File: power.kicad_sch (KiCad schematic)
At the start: 55 parts, among them T1 net-tie, U1 LMR54410, U11 RT9080-33GJ5, U3 TPS546D24ARVFR, U5 MIC5504

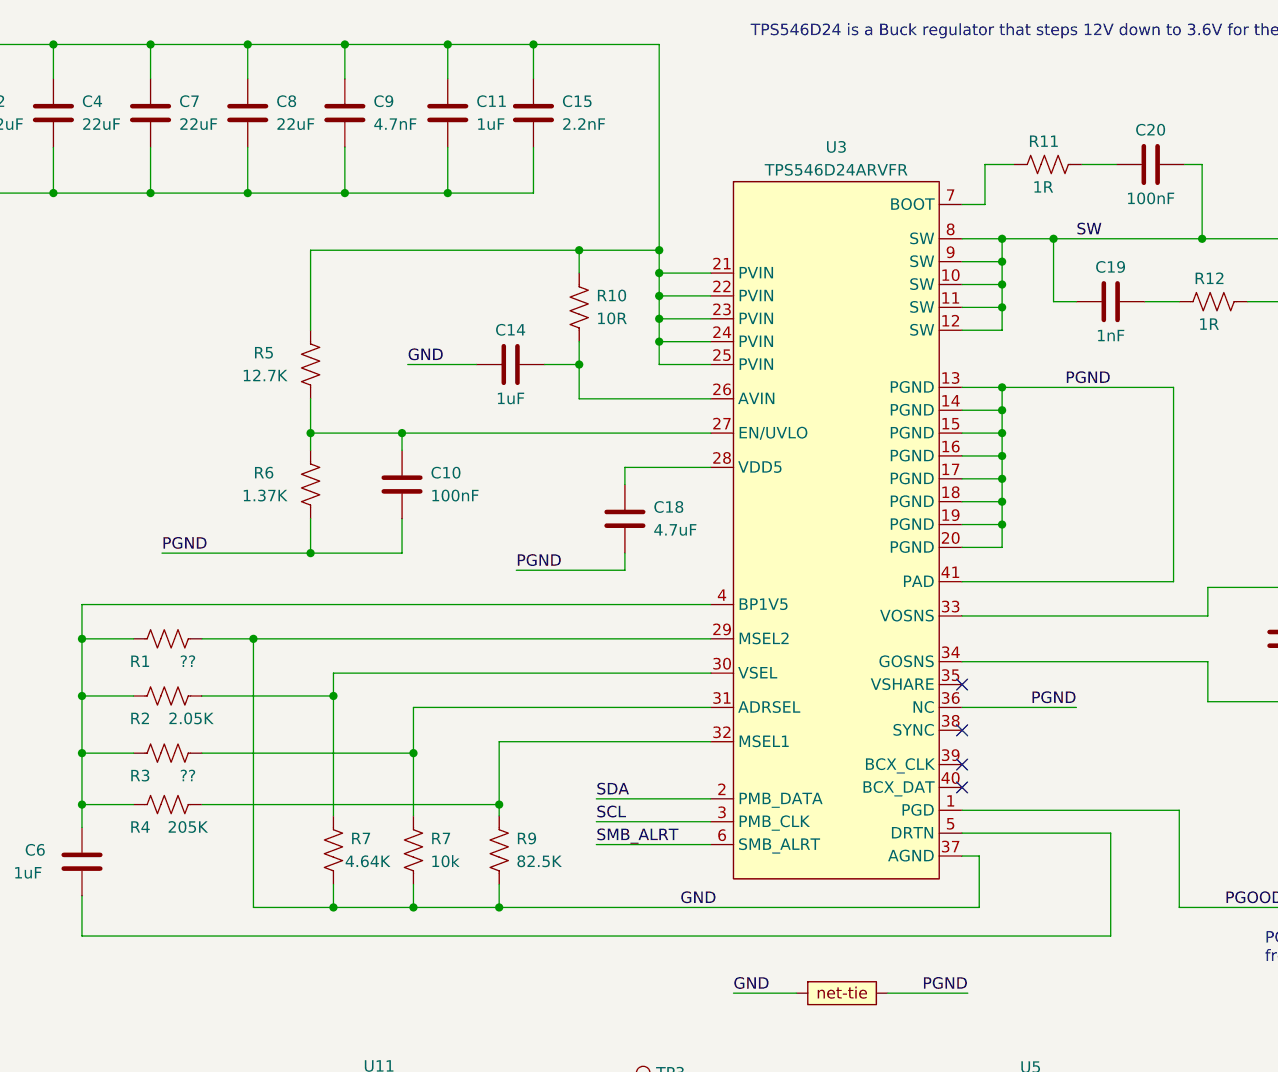
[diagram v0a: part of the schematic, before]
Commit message: more power supply routing
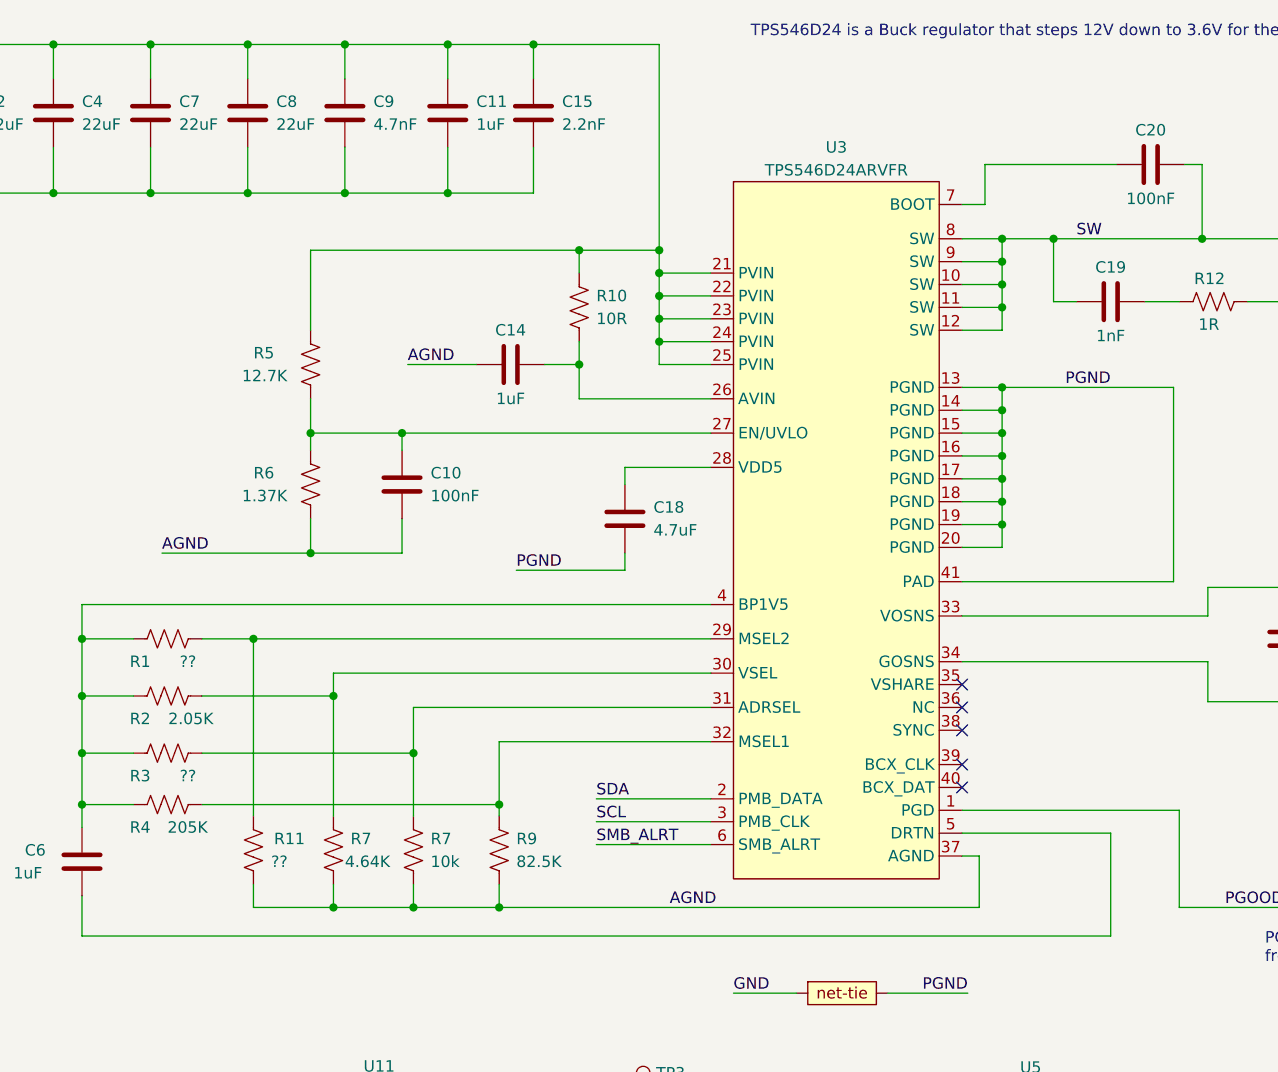
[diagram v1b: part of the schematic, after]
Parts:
- R11: value 1R -> ??
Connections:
- net GND: no longer C14.1, R1.2, R7.1, R7.2, R9.2, U3.29 (MSEL2), U3.37 (AGND)
- net PGND: no longer C10.2, R6.2, U3.36 (NC)
- net at C20.1: now also U3.7 (BOOT); no longer R11.2
- net AGND: now reaches R11.1
- net AGND: now also C10.2, C14.1, R6.2, R7.1, R7.2, R9.2, U3.37 (AGND); no longer U3.7 (BOOT)
- new net: R1.2, R11.2, U3.29 (MSEL2)
- no-connect marks 5 -> 6

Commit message: More power supply stuff
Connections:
- net AGND: now also T1.
- net GND: no longer T1.
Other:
- note added: "Connect at U3 Pin 37"
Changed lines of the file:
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@@
+    (effects (font (size 1.27 1.27)) (justify left bottom))
+  )
+  (text "Connect at\nU3 Pin 37" (at 139.7 131.445 0)
     (effects (font (size 1.27 1.27)) (justify left bottom))
   )
@@
     (effects (font (size 1.27 1.27)) (justify left bottom))
   )
-  (label "GND" (at 132.715 125.73 0) (fields_autoplaced)
+  (label "AGND" (at 132.715 125.73 0) (fields_autoplaced)
     (effects (font (size 1.27 1.27)) (justify left bottom))
   )

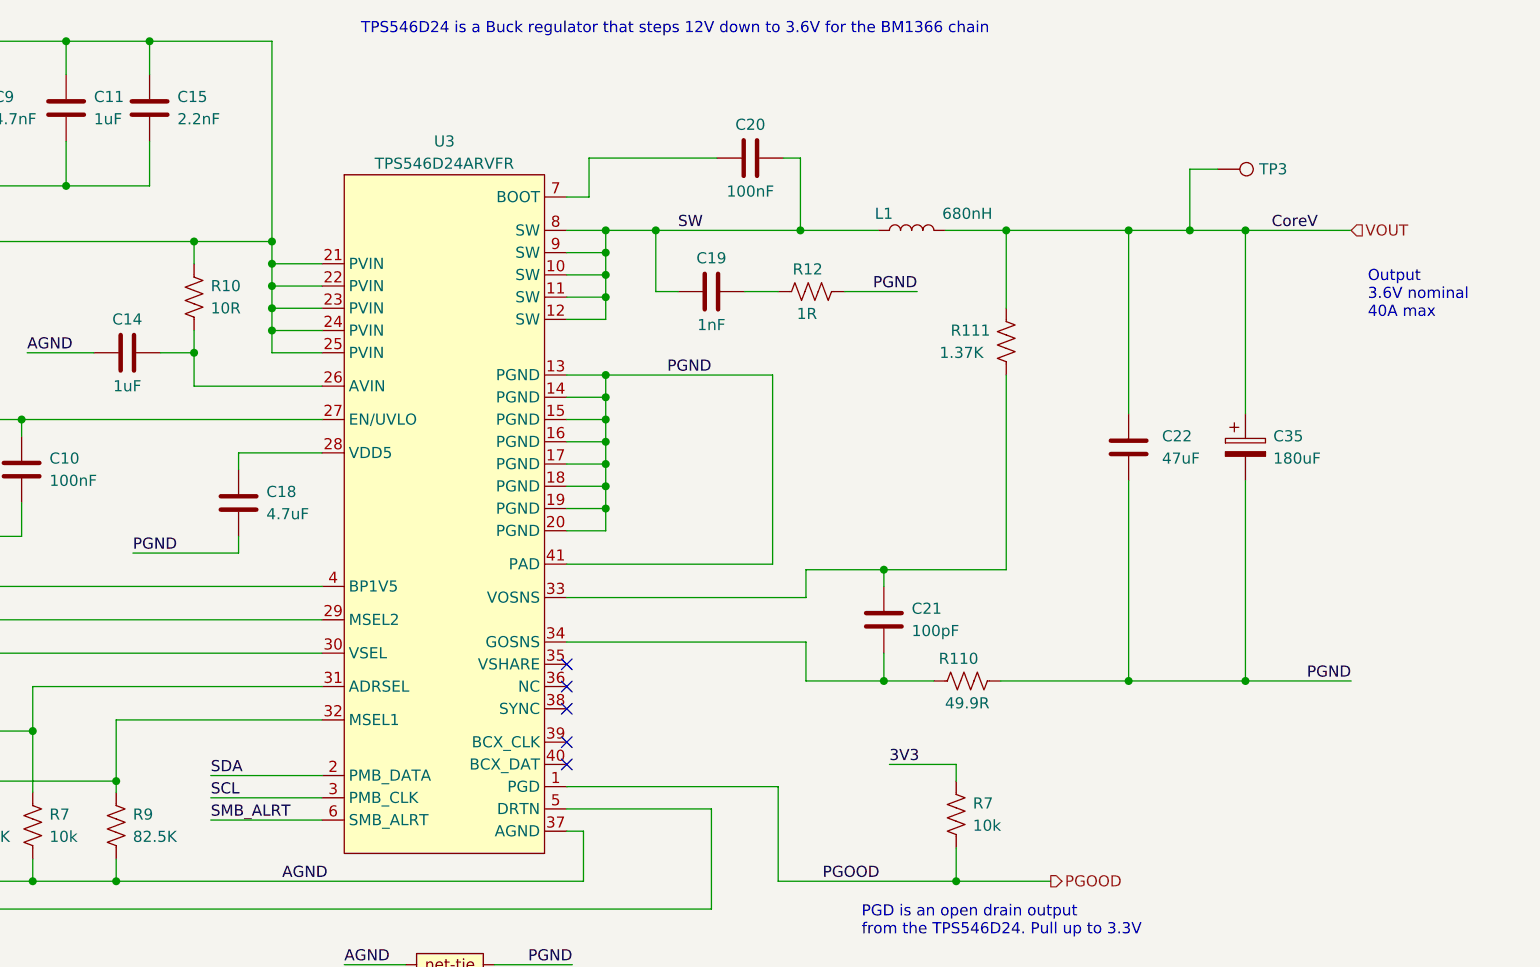
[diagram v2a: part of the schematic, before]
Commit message: reshuffle power supply planes
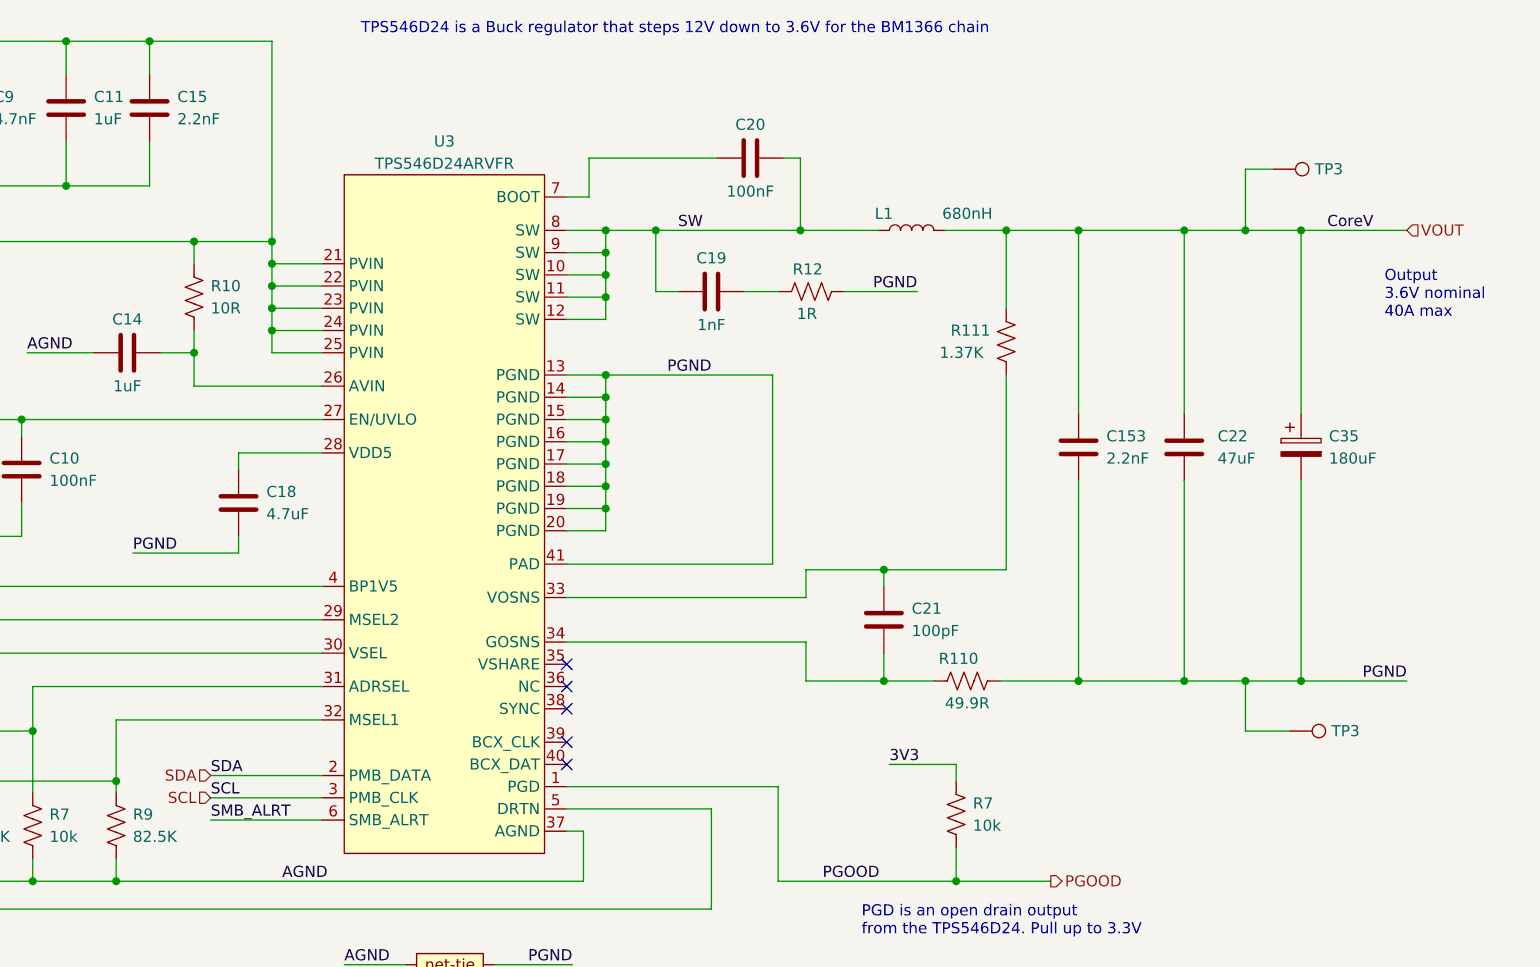
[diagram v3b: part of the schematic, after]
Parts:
- added C153: 2.2nF, Capacitor_SMD:C_0402_1005Metric, symbol Device:C
- added TP3: TestPoint, TestPoint:TestPoint_Pad_D1.0mm, symbol Connector:TestPoint
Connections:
- net PGND: now also C153.2, TP3.1
- net VOUT: now also C153.1
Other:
- moved on the sheet: C22, C35, TP3

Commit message: more routing
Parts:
- added C154: 47uF, Capacitor_SMD:C_1210_3225Metric, symbol Device:C
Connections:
- net PGND is gone; now on net GND: C11.2, C15.2, C153.2, C18.2, C2.2, C22.2, C35.2, C35.2, C4.2, C7.2, C8.2, C9.2, R110.2, R12.2, T1., TP3.1, U3.13 (PGND), U3.14 (PGND), U3.15 (PGND), U3.16 (PGND), U3.17 (PGND), U3.18 (PGND), U3.19 (PGND), U3.20 (PGND), U3.41 (PAD)
- net GND: now also C154.2
- net VOUT: now also C154.1
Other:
- moved on the sheet: C153, C22, C35, C6, R1, R11, R111, R2, R3, R4, R7, R9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

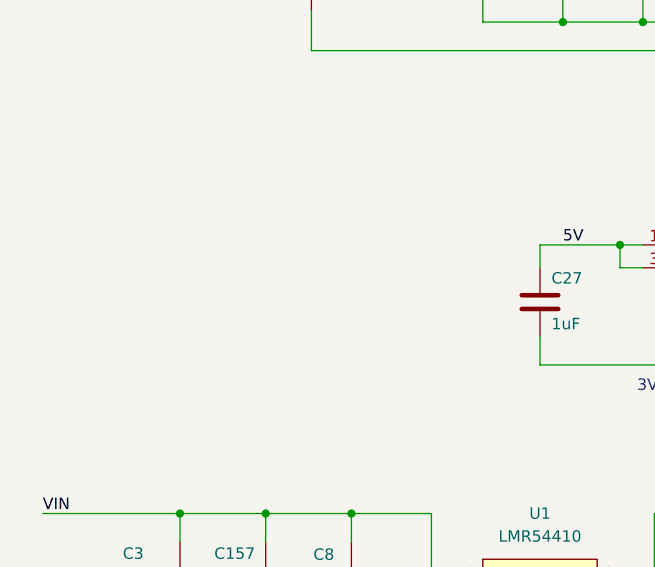
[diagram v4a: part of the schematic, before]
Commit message: Finish initial routing pass
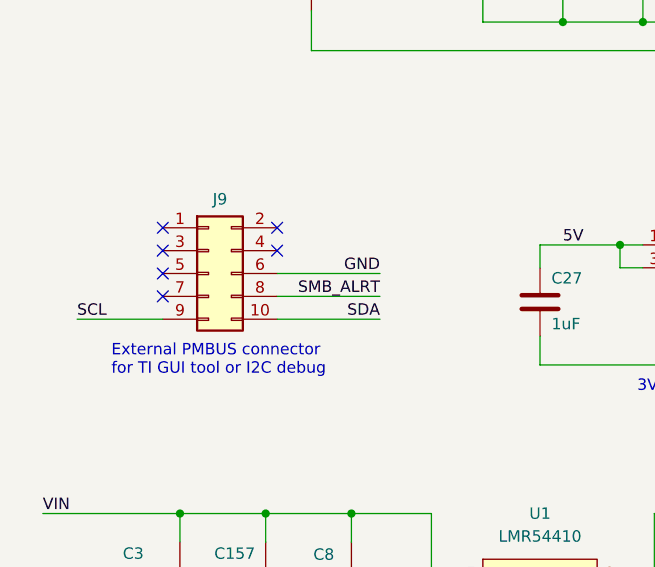
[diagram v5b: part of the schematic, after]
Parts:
- added J9: Conn_02x05_Odd_Even, Connector_PinHeader_2.54mm:PinHeader_2x05_P2.54mm_Vertical, symbol Connector_Generic:Conn_02x05_Odd_Even
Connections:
- net GND: now also J9.6 (Pin_6)
- net SCL: now also J9.9 (Pin_9)
- net SDA: now also J9.10 (Pin_10)
- net SMB_ALRT: now also J9.8 (Pin_8)
- no-connect marks 6 -> 12
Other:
- note added: "External PMBUS connector for TI GUI tool or I2C debug"
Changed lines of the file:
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@@
   )
   (no_connect (at 158.115 102.87))
+  (no_connect (at 43.815 141.605))
   (no_connect (at 102.235 143.51))
   (no_connect (at 158.115 96.52))
+  (no_connect (at 43.815 139.065))
+  (no_connect (at 31.115 139.065))
+  (no_connect (at 31.115 146.685))
+  (no_connect (at 31.115 141.605))
+  (no_connect (at 31.115 144.145))
   (no_connect (at 158.115 91.44))
   (no_connect (at 158.115 100.33))
@@
     (stroke (width 0) (type default))
   )
+  (wire (pts (xy 21.59 149.225) (xy 31.115 149.225))
+    (stroke (width 0) (type default))
+  )
   (wire (pts (xy 120.65 67.31) (xy 130.175 67.31))
     (stroke (width 0) (type default))
@@
     (stroke (width 0) (type default))
   )
+  (wire (pts (xy 43.815 146.685) (xy 55.245 146.685))
+    (stroke (width 0) (type default))
+  )
   (wire (pts (xy 162.56 60.96) (xy 162.56 63.5))
     (stroke (width 0) (type default))
@@
     (stroke (width 0) (type default))
   )
+  (wire (pts (xy 43.815 144.145) (xy 55.245 144.145))
+    (stroke (width 0) (type default))
+  )
   (wire (pts (xy 212.09 41.91) (xy 224.155 41.91))
     (stroke (width 0) (type default))
@@
   )
   (wire (pts (xy 174.625 141.605) (xy 183.515 141.605))
+    (stroke (width 0) (type default))
+  )
+  (wire (pts (xy 43.815 149.225) (xy 55.245 149.225))
     (stroke (width 0) (type default))
   )
@@
     (effects (font (size 1.27 1.27)) (justify left bottom))
   )
+  (text "External PMBUS connector\nfor TI GUI tool or I2C debug"
+    (at 25.4 155.575 0)
+    (effects (font (size 1.27 1.27)) (justify left bottom))
+  )
   (text "600 mA max" (at 121.285 144.78 0)
     (effects (font (size 1.27 1.27)) (justify left bottom))
@@
     (effects (font (size 1.27 1.27)) (justify right bottom))
   )
+  (label "SMB_ALRT" (at 55.245 146.685 180) (fields_autoplaced)
+    (effects (font (size 1.27 1.27)) (justify right bottom))
+  )
   (label "AGND" (at 130.81 116.205 180) (fields_autoplaced)
     (effects (font (size 1.27 1.27)) (justify right bottom))
@@
     (effects (font (size 1.27 1.27)) (justify left bottom))
   )
+  (label "SCL" (at 21.59 149.225 0) (fields_autoplaced)
+    (effects (font (size 1.27 1.27)) (justify left bottom))
+  )
   (label "SCL" (at 117.475 106.68 0) (fields_autoplaced)
     (effects (font (size 1.27 1.27)) (justify left bottom))
   )
+  (label "SDA" (at 55.245 149.225 180) (fields_autoplaced)
+    (effects (font (size 1.27 1.27)) (justify right bottom))
+  )
   (label "VIN" (at 17.78 170.815 0) (fields_autoplaced)
     (effects (font (size 1.27 1.27)) (justify left bottom))
@@
   (label "5V" (at 125.73 170.815 0) (fields_autoplaced)
     (effects (font (size 1.27 1.27)) (justify left bottom))
+  )
+  (label "GND" (at 55.245 144.145 180) (fields_autoplaced)
+    (effects (font (size 1.27 1.27)) (justify right bottom))
   )
   (label "GND" (at 198.12 48.895 180) (fields_autoplaced)
@@
         )
       )
+    )
+  )
+  (symbol (lib_id "Connector_Generic:Conn_02x05_Odd_Even") (at 36.195 144.145 0) (unit 1)
+    (in_bom yes) (on_board yes) (dnp no) (fields_autoplaced)
+    (property "Reference" "J9" (at 37.465 135.89 0)
+      (effects (font (size 1.27 1.27)))
+    )
+    (property "Value" "Conn_02x05_Odd_Even" (at 37.465 135.89 0)
+      (effects (font (size 1.27 1.27)) hide)
+    )
+    (property "Footprint" "Connector_PinHeader_2.54mm:PinHeader_2x05_P2.54mm_Vertical" (at 36.195 144.145 0)
+      (effects (font (size 1.27 1.27)) hide)
+    )
+    (property "Datasheet" "~" (at 36.195 144.145 0)
+      (effects (font (size 1.27 1.27)) hide)
+    )
+    (pin "1")
+    (pin "10")
+    (pin "2")
+    (pin "3")
+    (pin "4")
+    (pin "5")
+    (pin "6")
+    (pin "7")
+    (pin "8")
+    (pin "9")
+    (instances
+      (project "bitaxeHex"
+        (path "/e63e39d7-6ac0-4ffd-8aa3-1841a4541b55/8ec0a9c6-2b78-44ef-a83d-9047d2828409"
+          (reference "J9") (unit 1)
+        )
+      )

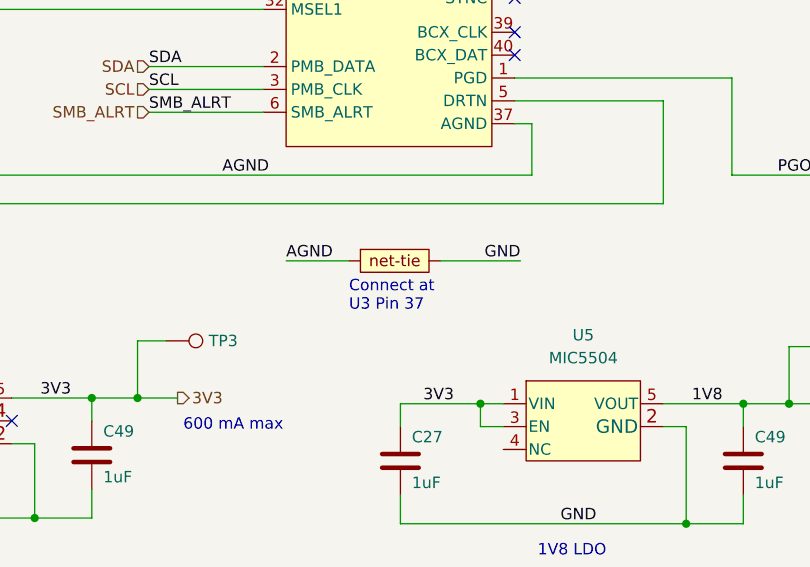
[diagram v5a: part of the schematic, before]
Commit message: connect AGND to GND
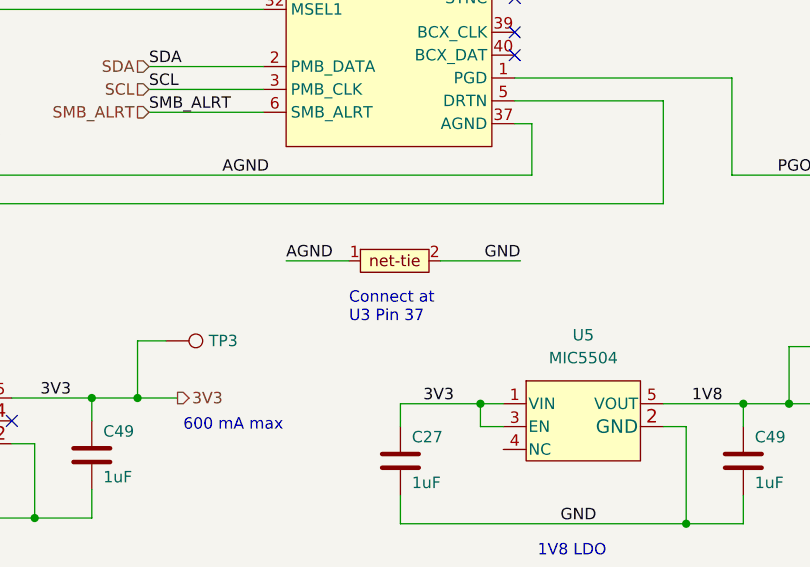
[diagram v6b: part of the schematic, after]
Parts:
- T1: footprint (none) -> bitaxe:Net-Tie-0.25mm
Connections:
- net AGND: now also T1.1; no longer T1.
- net GND: now also T1.2; no longer T1.
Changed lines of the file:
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@@
     (effects (font (size 1.27 1.27)) (justify left bottom))
   )
-  (text "Connect at\nU3 Pin 37" (at 139.7 131.445 0)
+  (text "Connect at\nU3 Pin 37" (at 139.7 132.715 0)
     (effects (font (size 1.27 1.27)) (justify left bottom))
   )
@@
       (effects (font (size 1.27 1.27)) hide)
     )
-    (property "Footprint" "" (at 143.51 127 0)
+    (property "Footprint" "bitaxe:Net-Tie-0.25mm" (at 143.51 127 0)
       (effects (font (size 1.27 1.27)) hide)
     )
@@
       (effects (font (size 1.27 1.27)) hide)
     )
-    (pin "")
-    (pin "")
-    (instances
-      (project "bitaxeHex"
+    (pin "1")
+    (pin "2")
+    (instances
+      (project "bitaxeHex"

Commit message: re-annotate all components
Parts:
- renumbered C9 to C1, C8 to C10, C3 to C11, C10 to C13, C11 to C14, C14 to C15, C15 to C16, C159 to C19, C156 to C20, C19 to C22, C20 to C23, C21 to C25, C153 to C26, C22 to C27, C154 to C28, C157 to C3, C2 to C4, C6 to C5, C4 to C7, C7 to C8, J9 to J3, L2 to L1, L1 to L2, R9 to R10, R112 to R11, R113 to R12, R10 to R13, R12 to R14, R110 to R16, R111 to R17, R11 to R5, R7 to R6, R5 to R8, R6 to R9, U5 to U4
